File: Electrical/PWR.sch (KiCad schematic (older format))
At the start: 53 parts

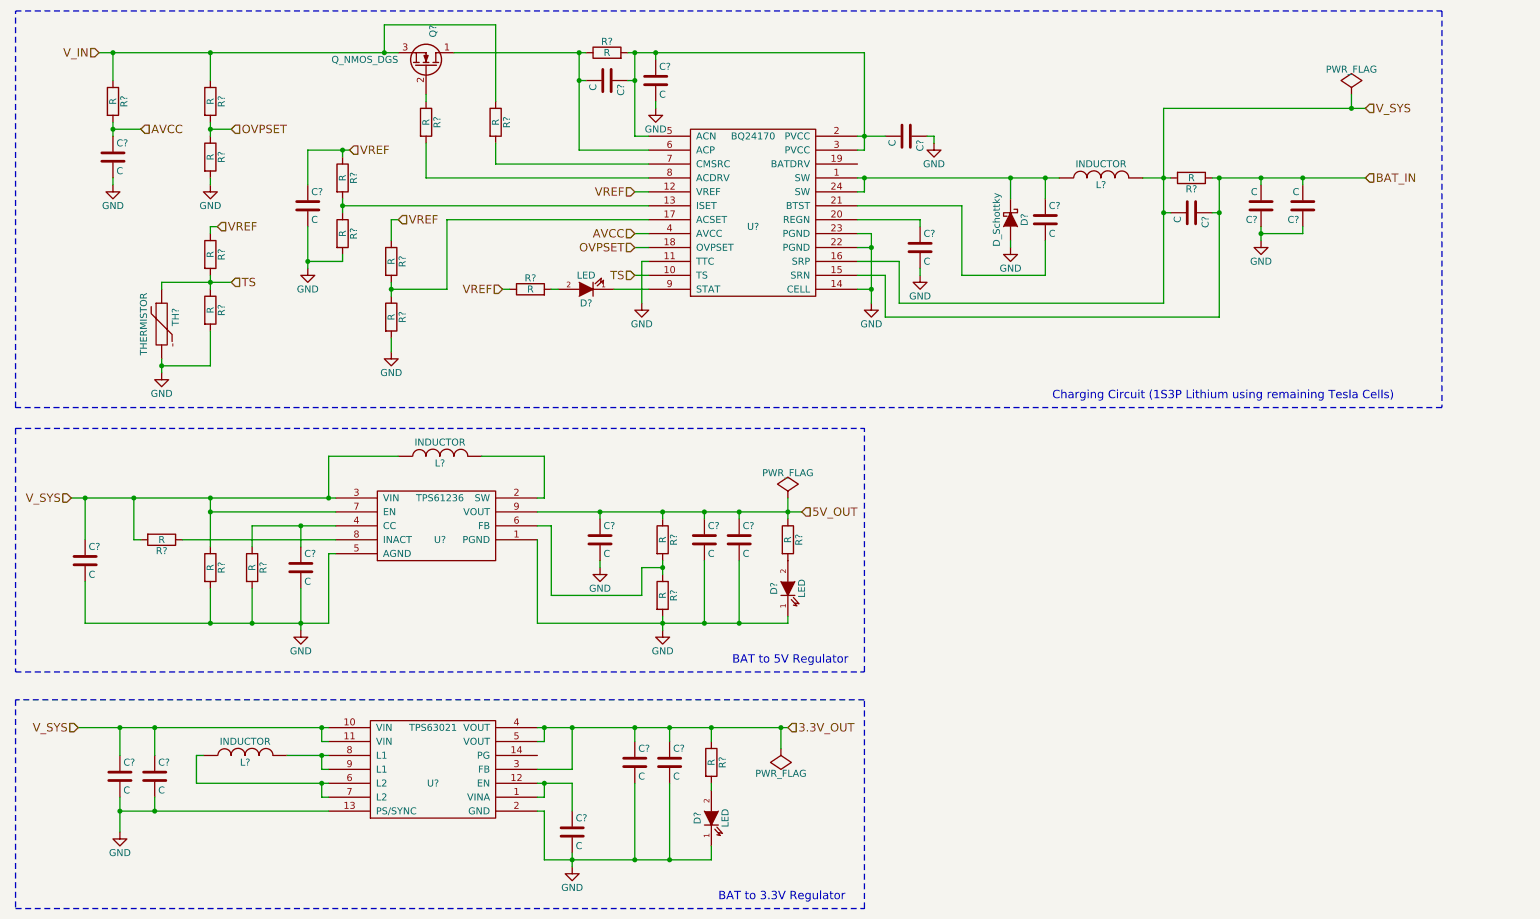
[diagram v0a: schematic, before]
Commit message: Finished power sheet
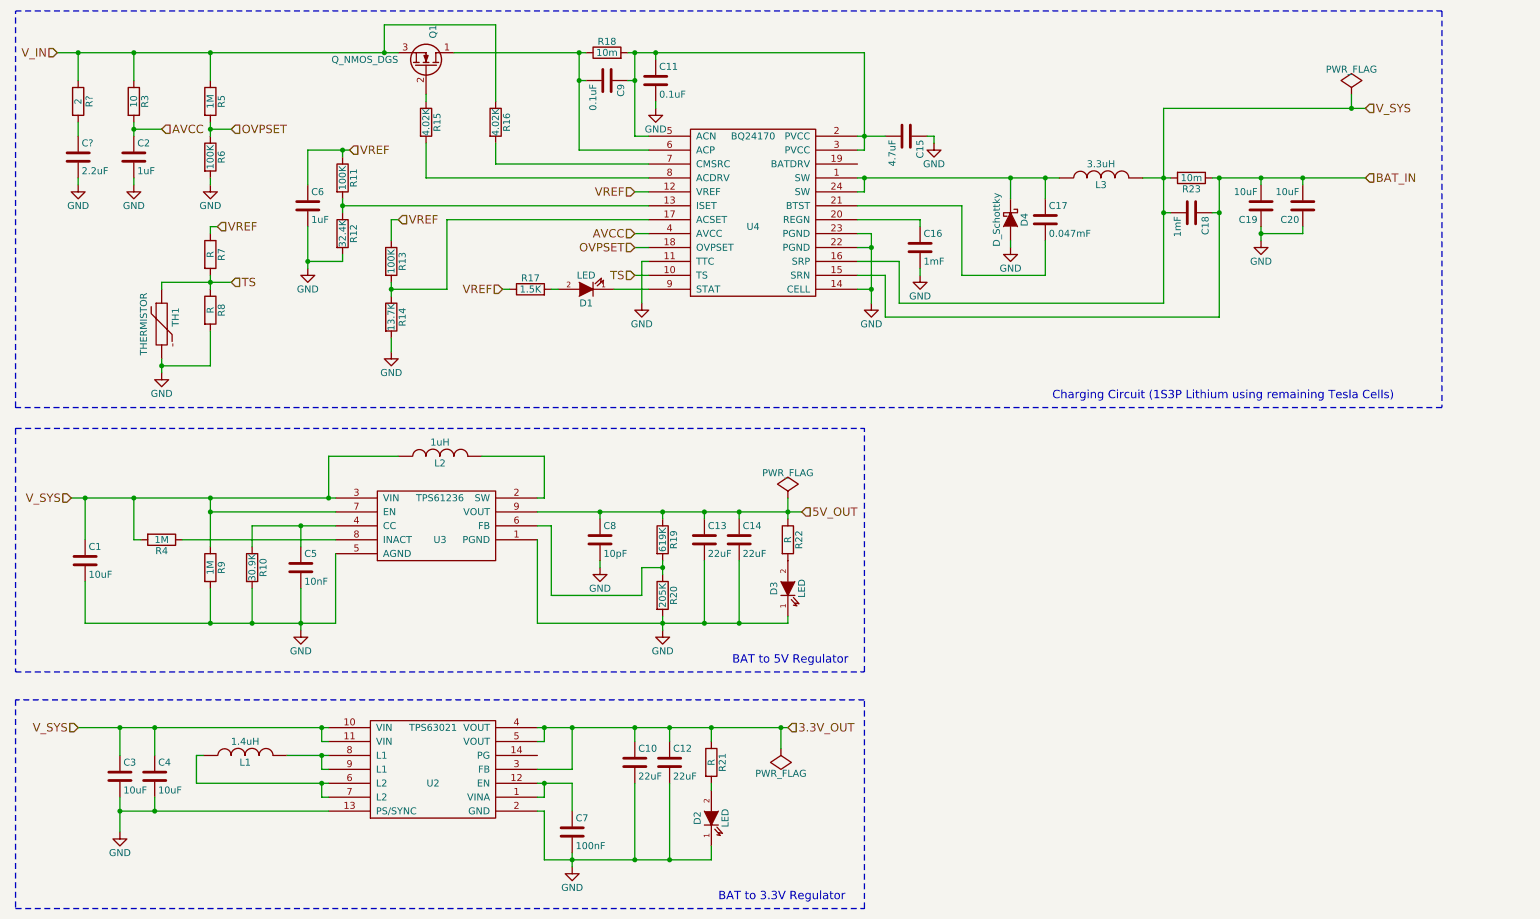
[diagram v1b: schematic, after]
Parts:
- added C?: 2.2uF, symbol C
- added R?: 2, symbol R
- C1, C19, C20, C3, C4: renamed from C?; value C -> 10uF
- C10, C12, C13, C14: renamed from C?; value C -> 22uF
- C11, C9: renamed from C?; value C -> 0.1uF
- C15: renamed from C?; value C -> 4.7uF
- C16, C18: renamed from C?; value C -> 1mF
- C17: renamed from C?; value C -> 0.047mF
- C2, C6: renamed from C?; value C -> 1uF
- C5: renamed from C?; value C -> 10nF
- C7: renamed from C?; value C -> 100nF
- C8: renamed from C?; value C -> 10pF
- L1: renamed from L?; value INDUCTOR -> 1.4uH
- L2: renamed from L?; value INDUCTOR -> 1uH
- L3: renamed from L?; value INDUCTOR -> 3.3uH
- R10: renamed from R?; value R -> 30.9K
- R11, R13, R6: renamed from R?; value R -> 100K
- R12: renamed from R?; value R -> 32.4K
- R14: renamed from R?; value R -> 13.7K
- R15, R16: renamed from R?; value R -> 4.02K
- R17: renamed from R?; value R -> 1.5K
- R18, R23: renamed from R?; value R -> 10m
- R19: renamed from R?; value R -> 619K
- R20: renamed from R?; value R -> 205K
- R3: renamed from R?; value R -> 10
- R4, R5, R9: renamed from R?; value R -> 1M
- gave numbers to parts that had none: 13
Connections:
- net GND: now also C?.2
- net V_IN: now also R?.1
- new net: C?.1, R?.2
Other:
- moved on the sheet: C2, R3

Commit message: schematic 95% donbe
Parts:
- C1, C10, C11, C12, C13, C14, C15, C3, C4: footprint (none) -> Capacitors_SMD:C_0805
- C16, C17, C19, C20: footprint (none) -> Capacitors_SMD:C_1206
- C18, C2, C5, C6, C7, C8, C9: footprint (none) -> Capacitors_SMD:C_0603
- C24: renamed from C?; footprint (none) -> Capacitors_SMD:C_0805
- D1, D2, D3: footprint (none) -> LEDs:LED_0603
- R10, R11, R12, R13, R14, R15, R16, R17, R19, R20, R21, R22, R3, R4, R5, R6, R7, R8, R9: footprint (none) -> Resistors_SMD:R_0603
- R18, R23: footprint (none) -> Resistors_SMD:R_1206
- R24: renamed from R?; footprint (none) -> Resistors_SMD:R_1206
- TH1: footprint (none) -> Connect:PINHEAD1-2
- U2: footprint MODULE -> Snow_parts:R-PVSON-N14
- U3: footprint MODULE -> Snow_parts:VQFN-9
- U4: footprint MODULE -> Snow_parts:pvqfn-n24
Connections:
- net GND: no longer C8.2
- net at R19.2, R20.1, U3.6 (FB): now also C8.2

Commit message: schematic 95% done
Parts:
- C16: value 1mF -> 1uF; footprint Capacitors_SMD:C_1206 -> Capacitors_SMD:C_0603
- C17: value 0.047mF -> 0.047uF; footprint Capacitors_SMD:C_1206 -> Capacitors_SMD:C_0603
- C18: value 1mF -> 0.1uF
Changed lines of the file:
@@
 P 8100 2100
 F 0 "C17" H 8125 2200 50  0000 L CNN
-F 1 "0.047mF" H 8125 2000 50  0000 L CNN
-F 2 "Capacitors_SMD:C_1206" H 8138 1950 50  0001 C CNN
+F 1 "0.047uF" H 8125 2000 50  0000 L CNN
+F 2 "Capacitors_SMD:C_0603" H 8138 1950 50  0001 C CNN
 F 3 "" H 8100 2100 50  0000 C CNN
 	1    8100 2100
@@
 P 9150 2050
 F 0 "C18" H 9175 2150 50  0000 L CNN
-F 1 "1mF" H 9175 1950 50  0000 L CNN
+F 1 "0.1uF" H 9175 1950 50  0000 L CNN
 F 2 "Capacitors_SMD:C_0603" H 9188 1900 50  0001 C CNN
 F 3 "" H 9150 2050 50  0000 C CNN
@@
 P 7200 2300
 F 0 "C16" H 7225 2400 50  0000 L CNN
-F 1 "1mF" H 7225 2200 50  0000 L CNN
-F 2 "Capacitors_SMD:C_1206" H 7238 2150 50  0001 C CNN
+F 1 "1uF" H 7225 2200 50  0000 L CNN
+F 2 "Capacitors_SMD:C_0603" H 7238 2150 50  0001 C CNN
 F 3 "" H 7200 2300 50  0000 C CNN
 	1    7200 2300

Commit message: minor tweaks
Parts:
- removed Q1: Q_NMOS_DGS, symbol Q_NMOS_DGS
- added Q1: CSD17313Q2, Snow_parts:WSON-FET-6, symbol CSD17313Q2
- D4: value D_Schottky -> FSV530AF; footprint (none) -> Snow_parts:DO-214AD
- L1: footprint (none) -> Snow_parts:SDR0403-1R4ML
- L2: footprint (none) -> Snow_parts:SRN8040-1R0Y
- L3: footprint (none) -> Snow_parts:SRP7030-3R3FM
- R21: value R -> 260
- R22: value R -> 600
- R3: footprint Resistors_SMD:R_0603 -> Resistors_SMD:R_1206
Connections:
- net V_IN: now also Q1.1 (D)
- net at C9.2, R18.1, U4.6 (ACP): now also Q1.3 (S)
- net at R15.1: now also Q1.2 (G)
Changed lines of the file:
@@
 F 0 "L3" V 8450 1800 50  0000 C CNN
 F 1 "3.3uH" V 8600 1800 50  0000 C CNN
-F 2 "" H 8500 1800 50  0001 C CNN
+F 2 "Snow_parts:SRP7030-3R3FM" H 8500 1800 50  0001 C CNN
 F 3 "" H 8500 1800 50  0000 C CNN
 	1    8500 1800
@@
 P 7850 2100
 F 0 "D4" H 7850 2200 50  0000 C CNN
-F 1 "D_Schottky" H 7850 2000 50  0000 C CNN
-F 2 "" H 7850 2100 50  0001 C CNN
+F 1 "FSV530AF" H 7850 2000 50  0000 C CNN
+F 2 "Snow_parts:DO-214AD" H 7850 2100 50  0001 C CNN
 F 3 "" H 7850 2100 50  0000 C CNN
 	1    7850 2100
@@
 $EndComp
 $Comp
-L Q_NMOS_DGS Q1
-U 1 1 5847C952
-P 3650 1000
-F 0 "Q1" H 3950 1050 50  0000 R CNN
-F 1 "Q_NMOS_DGS" V 3700 800 50  0000 R CNN
-F 2 "" H 3850 1100 50  0001 C CNN
-F 3 "" H 3650 1000 50  0000 C CNN
-	1    3650 1000
-	0    1    -1   0
-$EndComp
-$Comp
 L R R15
 U 1 1 5847CD44
@@
 F 0 "R3" V 1630 1250 50  0000 C CNN
 F 1 "10" V 1550 1250 50  0000 C CNN
-F 2 "Resistors_SMD:R_0603" V 1480 1250 50  0001 C CNN
+F 2 "Resistors_SMD:R_1206" V 1480 1250 50  0001 C CNN
 F 3 "" H 1550 1250 50  0000 C CNN
 	1    1550 1250
@@
 F 0 "L2" V 3700 3800 50  0000 C CNN
 F 1 "1uH" V 3850 3800 50  0000 C CNN
-F 2 "" H 3750 3800 50  0001 C CNN
+F 2 "Snow_parts:SRN8040-1R0Y" H 3750 3800 50  0001 C CNN
 F 3 "" H 3750 3800 50  0000 C CNN
 	1    3750 3800
@@
 F 0 "L1" V 2300 5950 50  0000 C CNN
 F 1 "1.4uH" V 2450 5950 50  0000 C CNN
-F 2 "" H 2350 5950 50  0001 C CNN
+F 2 "Snow_parts:SDR0403-1R4ML" H 2350 5950 50  0001 C CNN
 F 3 "" H 2350 5950 50  0000 C CNN
 	1    2350 5950
@@
 P 6250 4400
 F 0 "R22" V 6330 4400 50  0000 C CNN
-F 1 "R" V 6250 4400 50  0000 C CNN
+F 1 "600" V 6250 4400 50  0000 C CNN
 F 2 "Resistors_SMD:R_0603" V 6180 4400 50  0001 C CNN
 F 3 "" H 6250 4400 50  0000 C CNN
@@
 P 5700 6000
 F 0 "R21" V 5780 6000 50  0000 C CNN
-F 1 "R" V 5700 6000 50  0000 C CNN
+F 1 "260" V 5700 6000 50  0000 C CNN
 F 2 "Resistors_SMD:R_0603" V 5630 6000 50  0001 C CNN
 F 3 "" H 5700 6000 50  0000 C CNN
@@
 	10150 1550 10150 1800
 Connection ~ 10150 1800
+$Comp
+L PWR_FLAG #FLG025
+U 1 1 585B7A25
+P 1050 850
+F 0 "#FLG025" H 1050 945 50  0001 C CNN
+F 1 "PWR_FLAG" H 1050 1030 50  0000 C CNN
+F 2 "" H 1050 850 50  0000 C CNN
+F 3 "" H 1050 850 50  0000 C CNN
+	1    1050 850
+	1    0    0    -1
+$EndComp
+Wire Wire Line
+	1050 850  1050 900
+Connection ~ 1050 900
+$Comp
+L CSD17313Q2 Q1
+U 1 1 585CA69C
+P 3650 1000
+F 0 "Q1" H 3950 1050 50  0000 R CNN
+F 1 "CSD17313Q2" V 3700 1650 50  0000 R CNN
+F 2 "Snow_parts:WSON-FET-6" H 3850 1100 50  0001 C CNN
+F 3 "" H 3650 1000 50  0000 C CNN
+	1    3650 1000
+	0    -1   -1   0
+$EndComp
 $EndSCHEMATC
